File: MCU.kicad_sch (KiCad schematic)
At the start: 11 parts, among them J1 Conn_ARM_JTAG_SWD_10, U1 STM32H725ZGT6, U2 M95P32-IXMNT_E, Y1 ABS05W-32.768KHZ-D-2-T, Y2 ECS-80-8-30Q-VY-TR

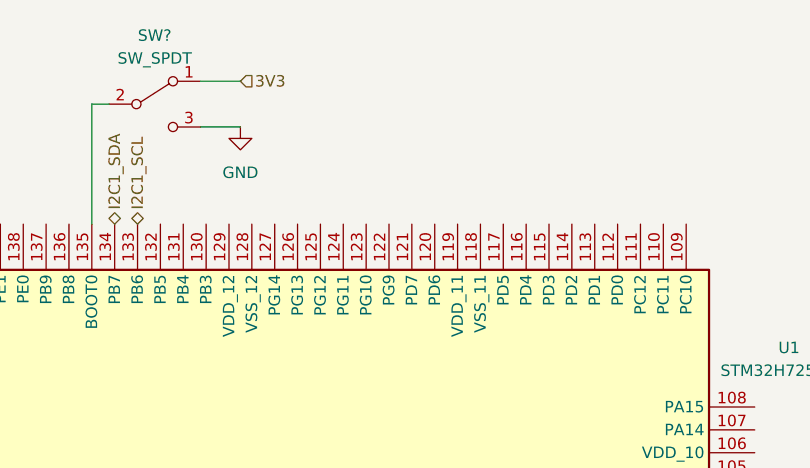
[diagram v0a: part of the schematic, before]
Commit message: MCU interfaces pulled out to parent sheet
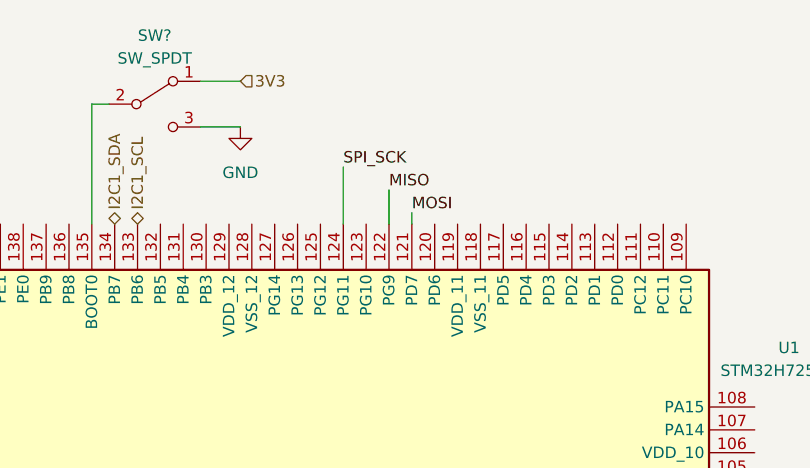
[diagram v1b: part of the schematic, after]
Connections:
- net MISO: now also U1.122 (PG9)
- net MOSI: now also U1.121 (PD7)
- net SPI_SCK: now also U1.124 (PG11)
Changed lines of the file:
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@@
+    (stroke (width 0) (type default) (color 0 0 0 0))
+  )
+  (wire (pts (xy 99.06 33.02) (xy 99.06 36.83))
     (stroke (width 0) (type default) (color 0 0 0 0))
   )
@@
   )
   (wire (pts (xy 217.17 27.94) (xy 220.98 27.94))
+    (stroke (width 0) (type default) (color 0 0 0 0))
+  )
+  (wire (pts (xy 93.98 30.48) (xy 93.98 36.83))
     (stroke (width 0) (type default) (color 0 0 0 0))
   )
@@
     (stroke (width 0) (type default) (color 0 0 0 0))
   )
+  (wire (pts (xy 101.6 35.56) (xy 101.6 36.83))
+    (stroke (width 0) (type default) (color 0 0 0 0))
+  )
   (wire (pts (xy 260.985 113.03) (xy 264.795 113.03))
     (stroke (width 0) (type default) (color 0 0 0 0))
@@
     (effects (font (size 1.27 1.27)) (justify right bottom))
   )
+  (label "MISO" (at 99.06 33.02 0)
+    (effects (font (size 1.27 1.27)) (justify left bottom))
+  )
+  (label "MOSI" (at 101.6 35.56 0)
+    (effects (font (size 1.27 1.27)) (justify left bottom))
+  )
   (label "HSE_OUT" (at 35.56 120.65 180)
     (effects (font (size 1.27 1.27)) (justify right bottom))
   )
+  (label "SPI_SCK" (at 93.98 30.48 0)
+    (effects (font (size 1.27 1.27)) (justify left bottom))
+  )
   (label "MOSI" (at 264.16 35.56 0)

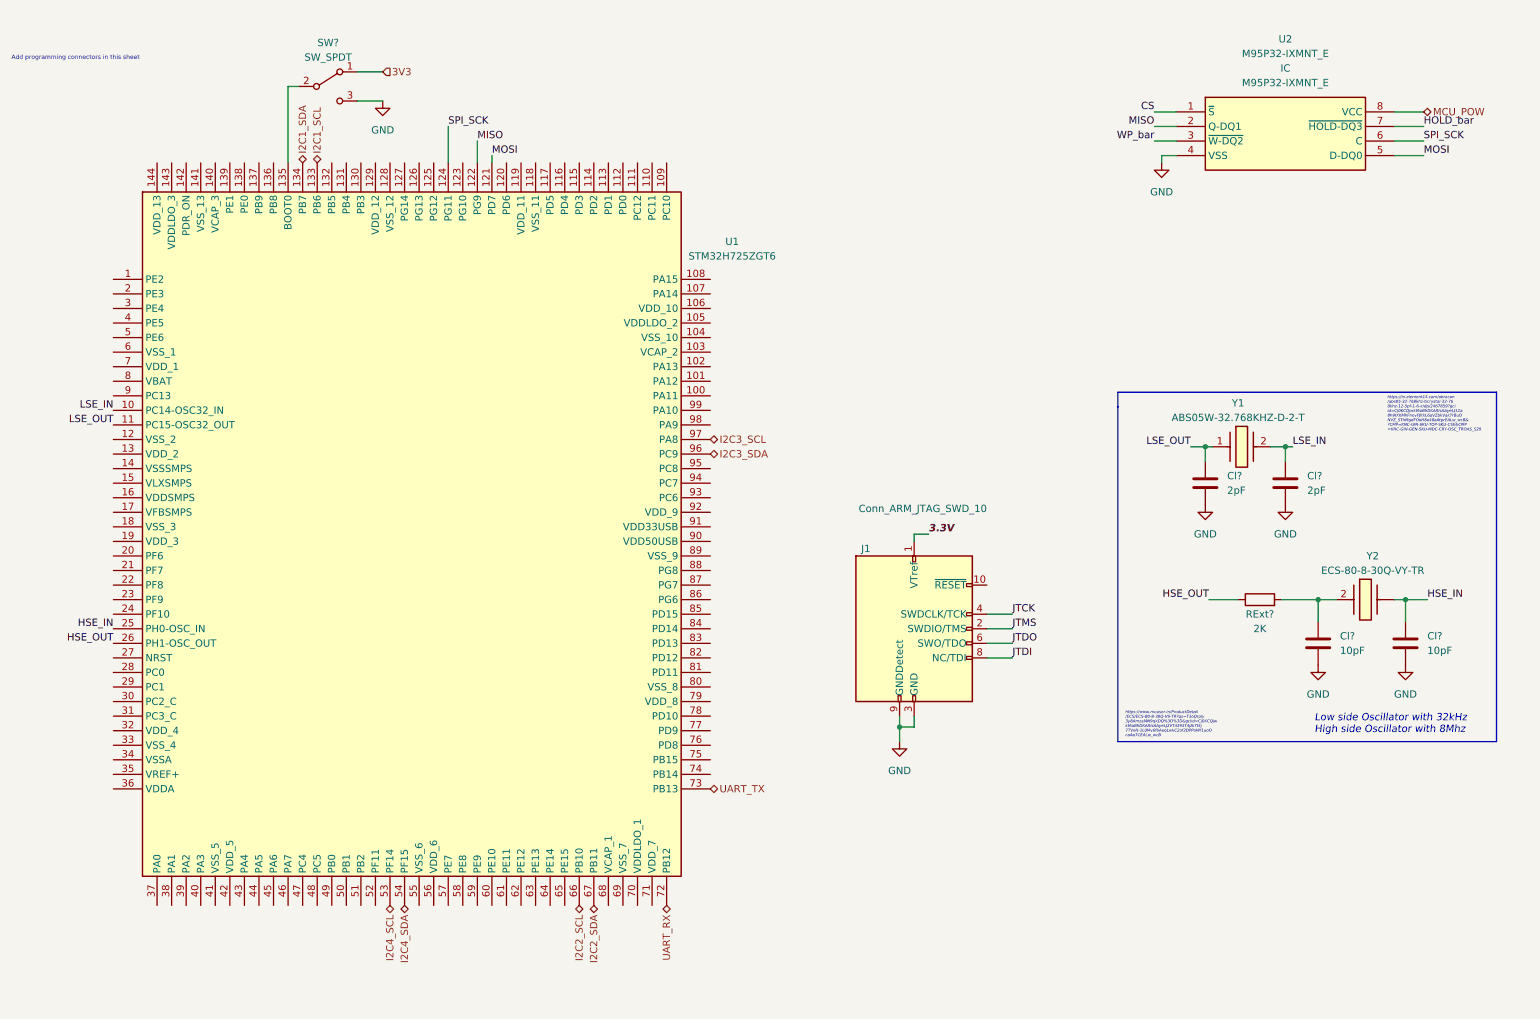
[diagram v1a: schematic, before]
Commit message: MCU interfaces are done! Check the Changes and Complete ERC modifications
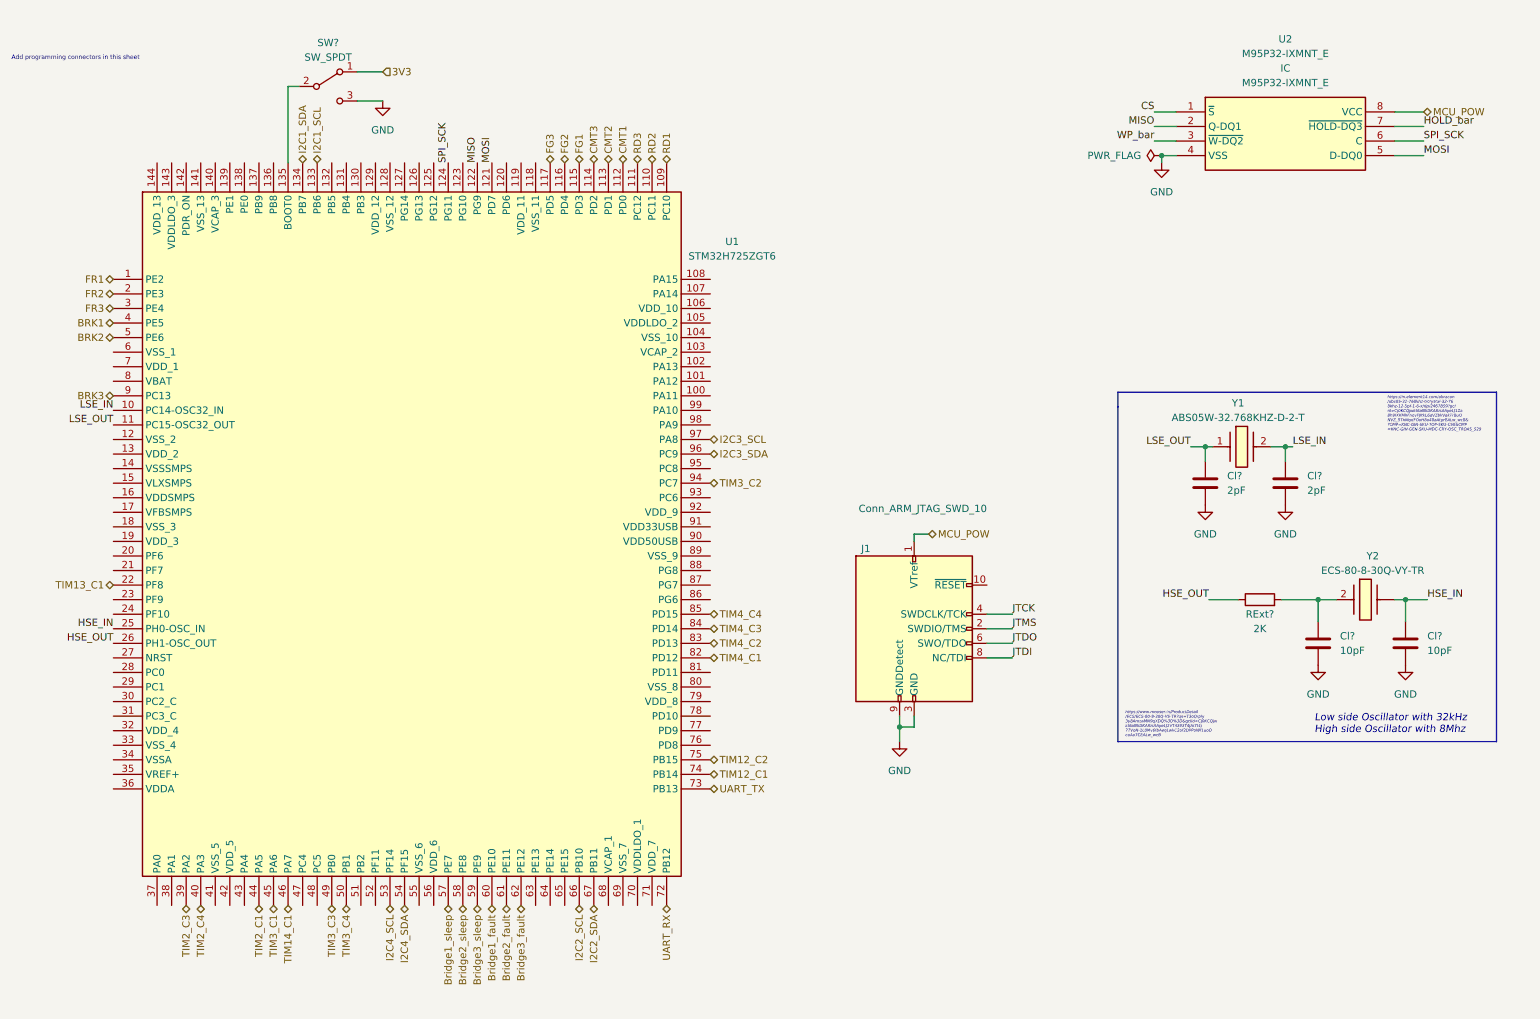
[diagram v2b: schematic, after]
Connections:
- net 3.3V is gone; now on net MCU_POW: J1.1 (VTref)
- net FR1: now reaches U1.1 (PE2)
- net RD1: now reaches U1.109 (PC10)
- net RD2: now reaches U1.110 (PC11)
- net RD3: now reaches U1.111 (PC12)
- net CMT1: now reaches U1.112 (PD0)
- net CMT2: now reaches U1.113 (PD1)
- net CMT3: now reaches U1.114 (PD2)
- net FG1: now reaches U1.115 (PD3)
- net FG2: now reaches U1.116 (PD4)
- net FG3: now reaches U1.117 (PD5)
- net FR2: now reaches U1.2 (PE3)
- net TIM13_C1: now reaches U1.22 (PF8)
- net FR3: now reaches U1.3 (PE4)
- net TIM2_C3: now reaches U1.39 (PA2)
- net BRK1: now reaches U1.4 (PE5)
- net TIM2_C4: now reaches U1.40 (PA3)
- net TIM2_C1: now reaches U1.44 (PA5)
- net TIM3_C1: now reaches U1.45 (PA6)
- net TIM14_C1: now reaches U1.46 (PA7)
- net TIM3_C3: now reaches U1.49 (PB0)
- net BRK2: now reaches U1.5 (PE6)
- net TIM3_C4: now reaches U1.50 (PB1)
- net Bridge1_sleep: now reaches U1.57 (PE7)
- net Bridge2_sleep: now reaches U1.58 (PE8)
- net Bridge3_sleep: now reaches U1.59 (PE9)
- net Bridge1_fault: now reaches U1.60 (PE10)
- net Bridge2_fault: now reaches U1.61 (PE11)
- net Bridge3_fault: now reaches U1.62 (PE12)
- net TIM12_C1: now reaches U1.74 (PB14)
- net TIM12_C2: now reaches U1.75 (PB15)
- net TIM4_C1: now reaches U1.82 (PD12)
- net TIM4_C2: now reaches U1.83 (PD13)
- net TIM4_C3: now reaches U1.84 (PD14)
- net TIM4_C4: now reaches U1.85 (PD15)
- net BRK3: now reaches U1.9 (PC13)
- net TIM3_C2: now reaches U1.94 (PC7)
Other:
- company: (none) -> Parikshit Student Satellite Team
- title: (none) -> AOCS BOARD

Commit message: Max ERC errors corrected
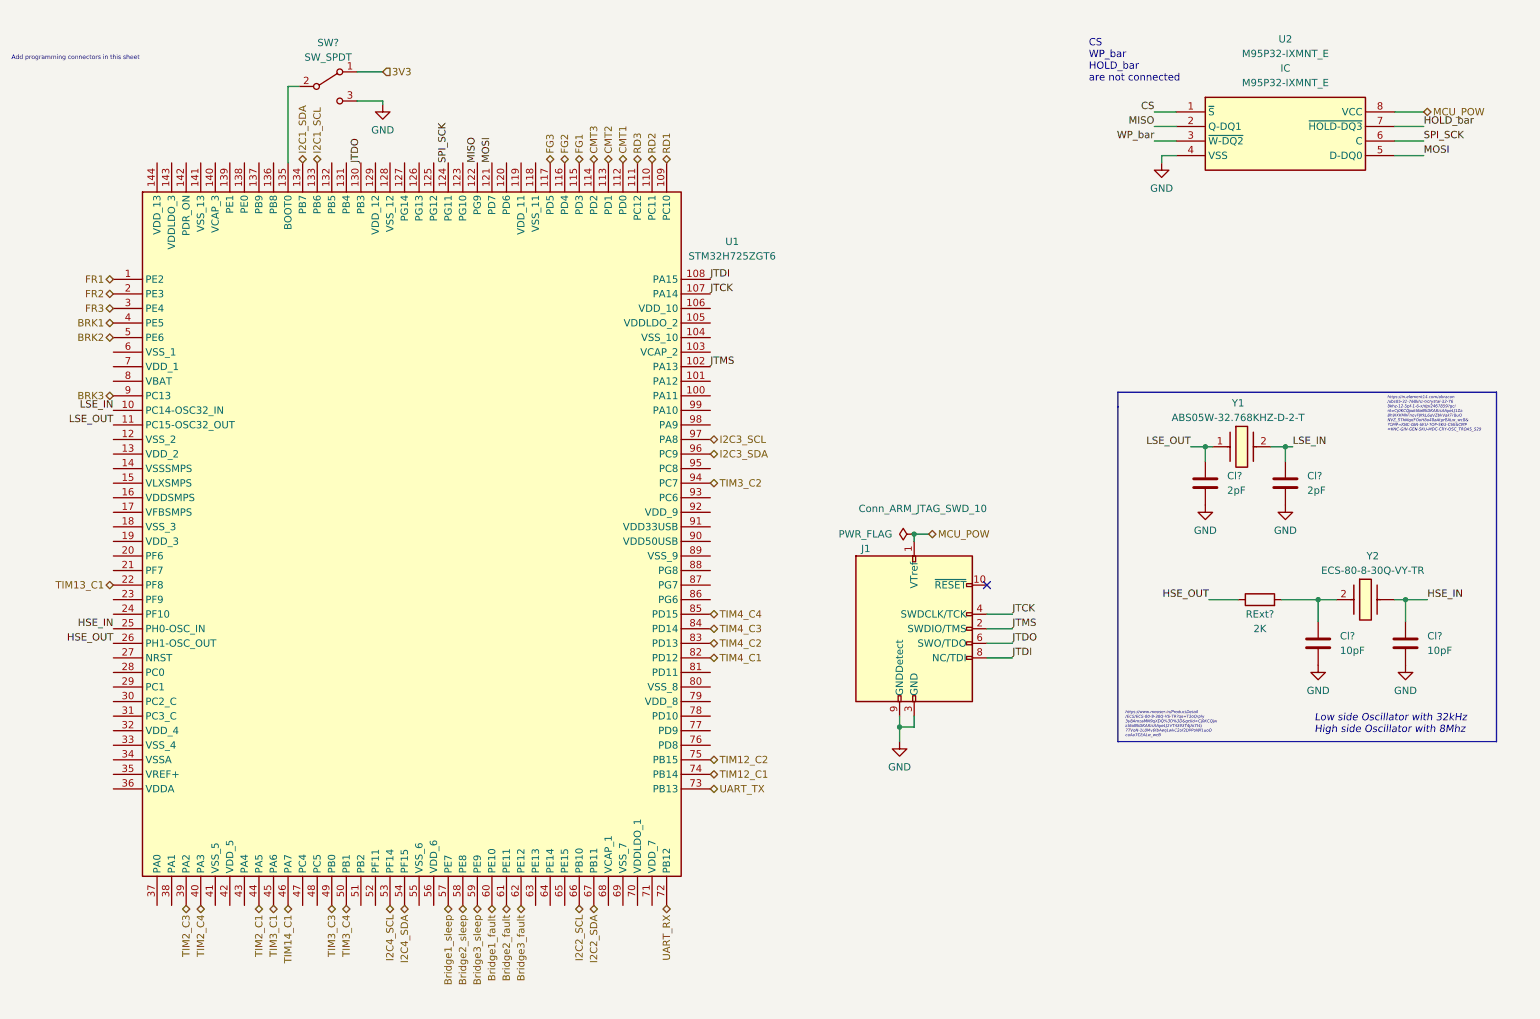
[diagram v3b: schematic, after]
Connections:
- net JTCK: now also U1.107 (PA14)
- net JTDI: now also U1.108 (PA15)
- net JTDO: now also U1.130 (PB3)
- net JTMS: now also U1.102 (PA13)
- no-connect marks 0 -> 1
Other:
- note added: "CS WP_bar HOLD_bar are not connected"

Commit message: Updated the changes
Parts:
- gave numbers to parts that had none: 6
- renumbered U1 to U3
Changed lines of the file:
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@@
   (symbol (lib_id "upsat-comms-hardware:GND") (at 82.55 26.67 0) (unit 1)
     (in_bom yes) (on_board yes) (fields_autoplaced)
-    (property "Reference" "#PWR0238" (id 0) (at 82.55 33.02 0)
+    (property "Reference" "#PWR015" (id 0) (at 82.55 33.02 0)
       (effects (font (size 1.27 1.27)) hide)
     )
@@
   (symbol (lib_id "Device:C") (at 245.745 120.65 0) (unit 1)
     (in_bom yes) (on_board yes)
-    (property "Reference" "Cl?" (id 0) (at 249.555 119.3799 0)
+    (property "Reference" "Cl3" (id 0) (at 249.555 119.3799 0)
       (effects (font (size 1.27 1.27)) (justify left))
     )
@@
   (symbol (lib_id "STM32H725ZGT6:STM32H725ZGT6") (at 35.56 57.15 0) (unit 1)
     (in_bom no) (on_board yes) (fields_autoplaced)
-    (property "Reference" "U1" (id 0) (at 143.51 50.5712 0))
+    (property "Reference" "U3" (id 0) (at 143.51 50.5712 0))
     (property "Value" "STM32H725ZGT6" (id 1) (at 143.51 53.1112 0))
     (property "Footprint" "STM32H725ZGT6:QFP50P2200X2200X160-144N" (id 2) (at 35.56 57.15 0)
@@
   (symbol (lib_id "upsat-comms-hardware:GND") (at 240.03 96.52 0) (unit 1)
     (in_bom yes) (on_board yes) (fields_autoplaced)
-    (property "Reference" "#PWR0115" (id 0) (at 240.03 102.87 0)
+    (property "Reference" "#PWR018" (id 0) (at 240.03 102.87 0)
       (effects (font (size 1.27 1.27)) hide)
     )
@@
   (symbol (lib_id "Device:R") (at 235.585 113.03 90) (unit 1)
     (in_bom yes) (on_board yes)
-    (property "Reference" "RExt?" (id 0) (at 235.585 115.57 90))
+    (property "Reference" "RExt1" (id 0) (at 235.585 115.57 90))
     (property "Value" "2K" (id 1) (at 235.585 118.11 90))
     (property "Footprint" "Resistor_SMD:R_0603_1608Metric" (id 2) (at 235.585 114.808 90)
@@
   (symbol (lib_id "Switch:SW_SPDT") (at 73.025 23.495 0) (unit 1)
     (in_bom yes) (on_board yes) (fields_autoplaced)
-    (property "Reference" "SW?" (id 0) (at 73.025 15.875 0))
+    (property "Reference" "SW1" (id 0) (at 73.025 15.875 0))
     (property "Value" "SW_SPDT" (id 1) (at 73.025 18.415 0))
     (property "Footprint" "" (id 2) (at 73.025 23.495 0)
@@
   (symbol (lib_id "upsat-comms-hardware:GND") (at 218.44 36.83 0) (unit 1)
     (in_bom yes) (on_board yes) (fields_autoplaced)
-    (property "Reference" "#PWR0237" (id 0) (at 218.44 43.18 0)
+    (property "Reference" "#PWR016" (id 0) (at 218.44 43.18 0)
       (effects (font (size 1.27 1.27)) hide)
     )
@@
   (symbol (lib_id "Device:C") (at 240.03 92.71 0) (unit 1)
     (in_bom yes) (on_board yes) (fields_autoplaced)
-    (property "Reference" "Cl?" (id 0) (at 243.84 91.4399 0)
+    (property "Reference" "Cl2" (id 0) (at 243.84 91.4399 0)
       (effects (font (size 1.27 1.27)) (justify left))
     )
@@
   (symbol (lib_id "upsat-comms-hardware:GND") (at 260.985 124.46 0) (unit 1)
     (in_bom yes) (on_board yes) (fields_autoplaced)
-    (property "Reference" "#PWR0116" (id 0) (at 260.985 130.81 0)
+    (property "Reference" "#PWR020" (id 0) (at 260.985 130.81 0)
       (effects (font (size 1.27 1.27)) hide)
     )
@@
   (symbol (lib_id "upsat-comms-hardware:GND") (at 226.06 96.52 0) (unit 1)
     (in_bom yes) (on_board yes) (fields_autoplaced)
-    (property "Reference" "#PWR0236" (id 0) (at 226.06 102.87 0)
+    (property "Reference" "#PWR017" (id 0) (at 226.06 102.87 0)
       (effects (font (size 1.27 1.27)) hide)
     )
@@
   (symbol (lib_id "upsat-comms-hardware:GND") (at 172.72 137.795 0) (unit 1)
     (in_bom yes) (on_board yes) (fields_autoplaced)
-    (property "Reference" "#PWR0118" (id 0) (at 172.72 144.145 0)
+    (property "Reference" "#PWR021" (id 0) (at 172.72 144.145 0)
       (effects (font (size 1.27 1.27)) hide)
     )
@@
   (symbol (lib_id "Device:C") (at 226.06 92.71 0) (unit 1)
     (in_bom yes) (on_board yes) (fields_autoplaced)
-    (property "Reference" "Cl?" (id 0) (at 229.87 91.4399 0)
+    (property "Reference" "Cl1" (id 0) (at 229.87 91.4399 0)
       (effects (font (size 1.27 1.27)) (justify left))
     )
@@
   (symbol (lib_id "power:PWR_FLAG") (at 175.26 101.6 90) (unit 1)
     (in_bom yes) (on_board yes) (fields_autoplaced)
-    (property "Reference" "#FLG0103" (id 0) (at 173.355 101.6 0)
+    (property "Reference" "#FLG04" (id 0) (at 173.355 101.6 0)
       (effects (font (size 1.27 1.27)) hide)
     )
@@
   (symbol (lib_id "Device:C") (at 260.985 120.65 0) (unit 1)
     (in_bom yes) (on_board yes) (fields_autoplaced)
-    (property "Reference" "Cl?" (id 0) (at 264.795 119.3799 0)
+    (property "Reference" "Cl4" (id 0) (at 264.795 119.3799 0)
       (effects (font (size 1.27 1.27)) (justify left))
     )
@@
   (symbol (lib_id "upsat-comms-hardware:GND") (at 245.745 124.46 0) (unit 1)
     (in_bom yes) (on_board yes) (fields_autoplaced)
-    (property "Reference" "#PWR0117" (id 0) (at 245.745 130.81 0)
-      (effects (font (size 1.27 1.27)) hide)
-    )
+    (property "Reference" "#PWR019" (id 0) (at 245.745 130.81 0)
+      (effects (font (size 1.27 1.27)) hide)
+    )
